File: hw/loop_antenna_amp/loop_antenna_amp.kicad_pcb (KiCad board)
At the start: 2 copper layers, 88.9 x 78.7 mm, 87 parts, among them J1 ANT1, J2 ANT2, J3 GND, J4 Coax (SMA), Q1 MMBT3904, Q2 MMBT3904, Q3 MMBT3904, Q4 MMBT3904, Q5 PZT3904, Q6 PZT3904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

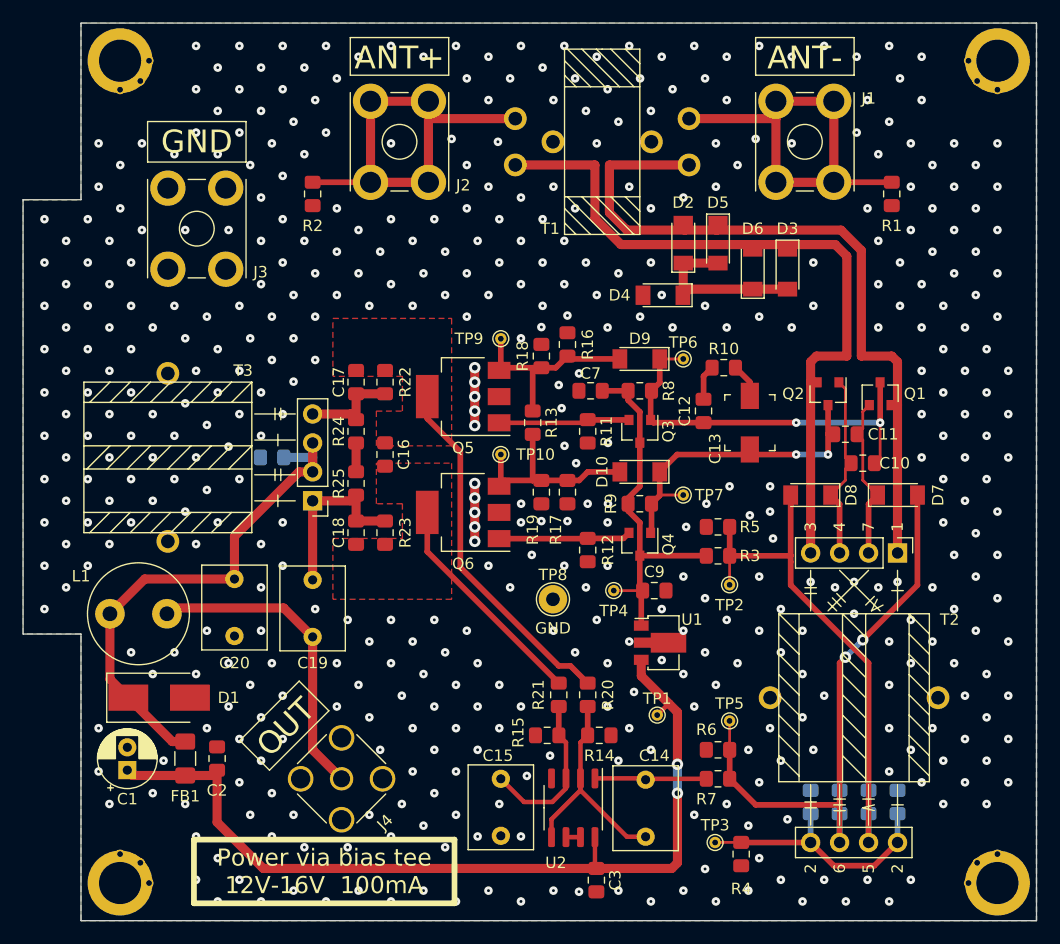
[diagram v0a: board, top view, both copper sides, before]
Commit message: Loop antenna amp: fix some vias
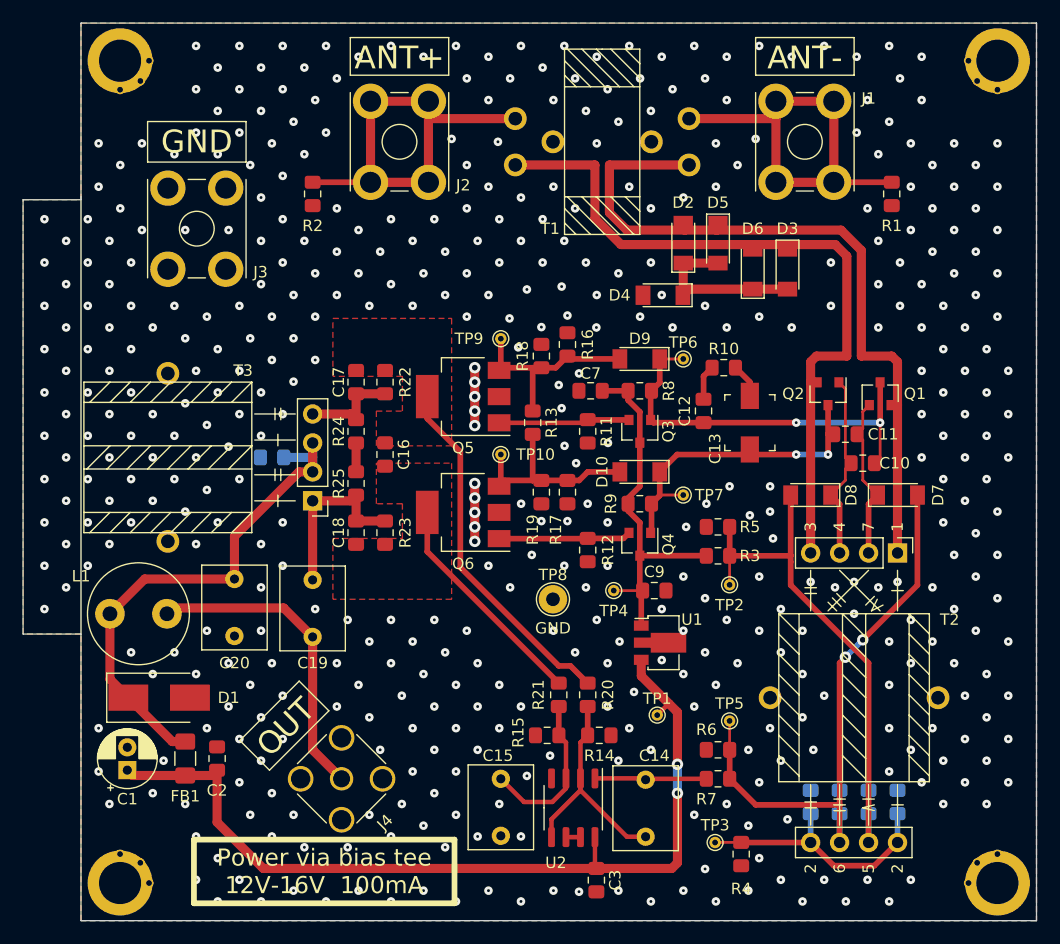
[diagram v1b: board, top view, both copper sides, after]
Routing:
- net GND: vias 483 -> 479

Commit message: Loop antenna amp: update PCB to match schematic, make it rectangular - remove fin
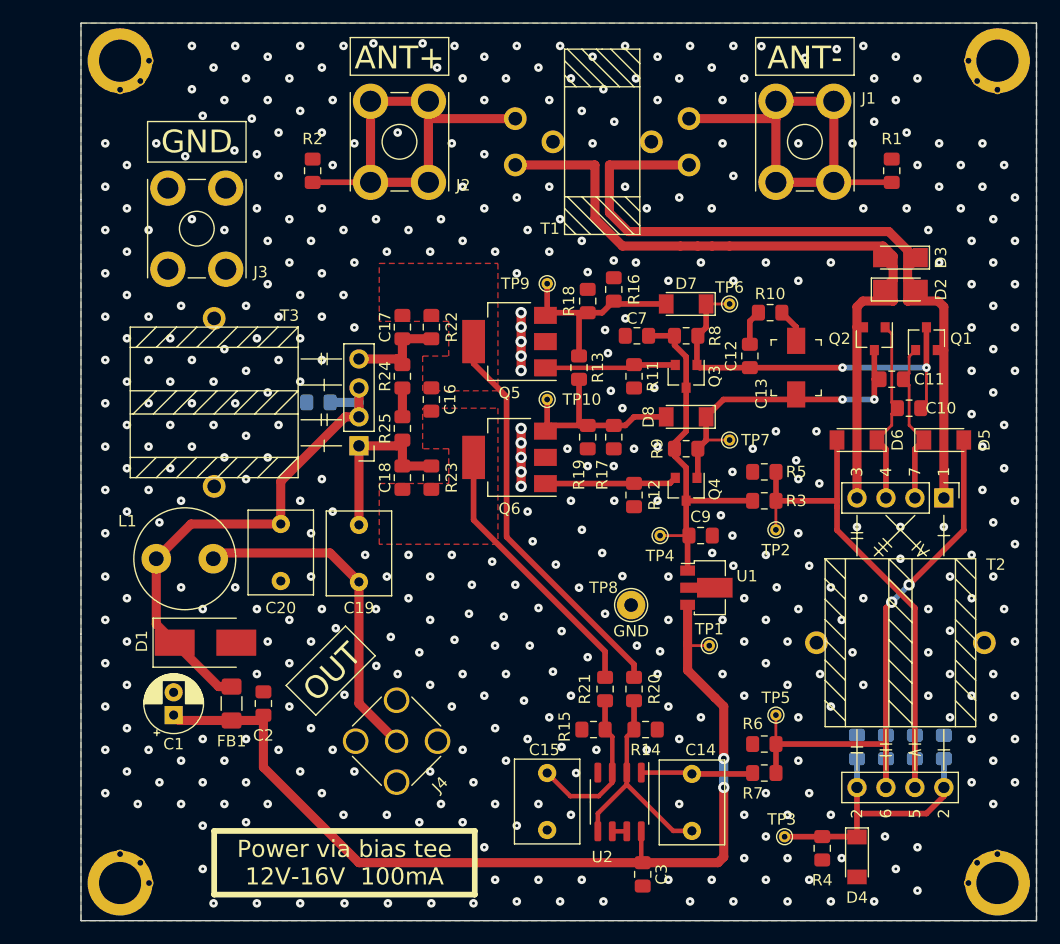
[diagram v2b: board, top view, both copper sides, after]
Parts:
- removed the D5 at (88.9, 72.4)
- removed the D6 at (91.9, 74.7)
- moved D4 52.1 mm to (101.1, 126.2), turned to 270 degrees
- moved D2 19.5 mm to (104.9, 76.5), turned to 0 degrees
- moved D3 9.96 mm to (104.9, 73.7), turned to 180 degrees
- moved TP1 7.62 mm to (88.1, 107.7)
- moved R4 7.13 mm to (98.0, 125.5)
- moved TP8 6.88 mm to (81.3, 104.1)
- moved C10 6.31 mm to (105.7, 86.9)
- moved C4 6.31 mm to (108.7, 116.6)
- moved C8 6.31 mm to (103.6, 116.6)
- moved C9 6.31 mm to (87.4, 98.0)
- moved R11 6.31 mm to (81.5, 84.1)
- moved R16 6.31 mm to (79.8, 76.5)
- moved T2 6.31 mm to (104.9, 107.4)
- moved TP10 6.31 mm to (73.9, 86.1)
- moved TP9 6.31 mm to (73.9, 75.9)
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- renumbered D7 to D5, D8 to D6, D9 to D7, D10 to D8
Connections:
- D3 pad 1: Net-(D3-Pad1) -> Net-(D2-Pad2)
- D4 pad 1: Net-(D2-Pad1) -> Net-(C4-Pad1)
- Q2 pad 2: Net-(D3-Pad1) -> Net-(D2-Pad1)
- T1 pad 3: Net-(D3-Pad1) -> Net-(D2-Pad1)
- T2 pad 3: Net-(D3-Pad1) -> Net-(D2-Pad1)
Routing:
- net Net-(D3-Pad1): track 65.6 -> 0.00 mm
- net Net-(D2-Pad1): track 15.3 -> 68.4 mm
- net VCC: track 78.5 -> 85.1 mm
- net Net-(C16-Pad2): track 19.8 -> 24.1 mm
- net Net-(D2-Pad2): track 66.0 -> 69.8 mm
- net Net-(C16-Pad1): track 31.6 -> 35.3 mm
- net Net-(C4-Pad1): track 22.8 -> 24.8 mm
- net Net-(C19-Pad1): track 27.5 -> 29.4 mm
- net Net-(C8-Pad1): track 51.5 -> 50.6 mm
- net GND: vias 479 -> 440
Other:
- board size 88.9 x 78.7 mm -> 83.8 x 78.7 mm

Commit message: Loop antenna amp: minor fixes of vias and silkscreen
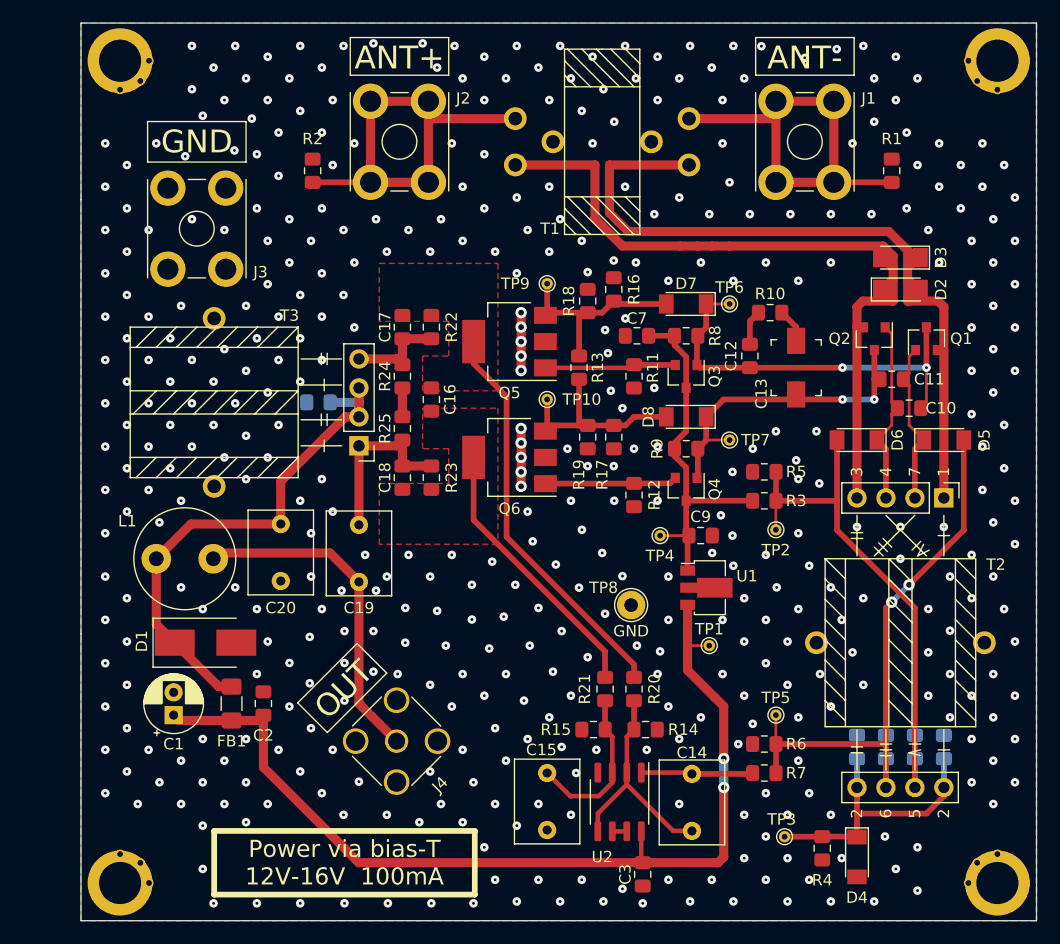
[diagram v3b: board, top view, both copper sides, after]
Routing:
- net GND: vias 440 -> 447
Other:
- board text added: "Power via bias-T 12V-16V 100mA"
- board text removed: "Power via bias tee 12V-16V 100mA"

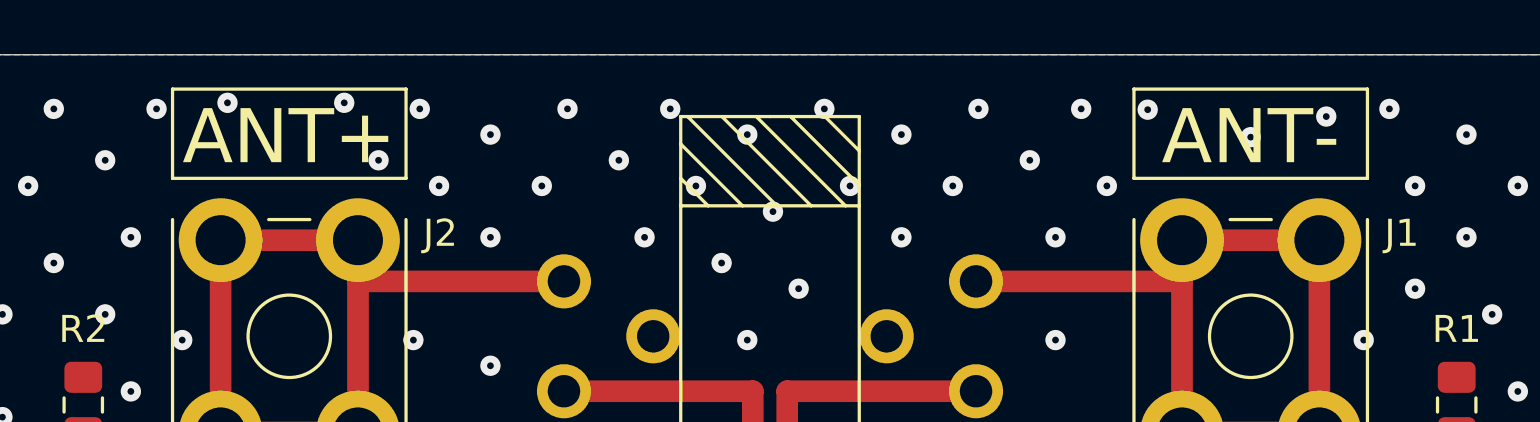
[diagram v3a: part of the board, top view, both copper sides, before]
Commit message: Loop antenna amp: fix antenna connector polarity markings
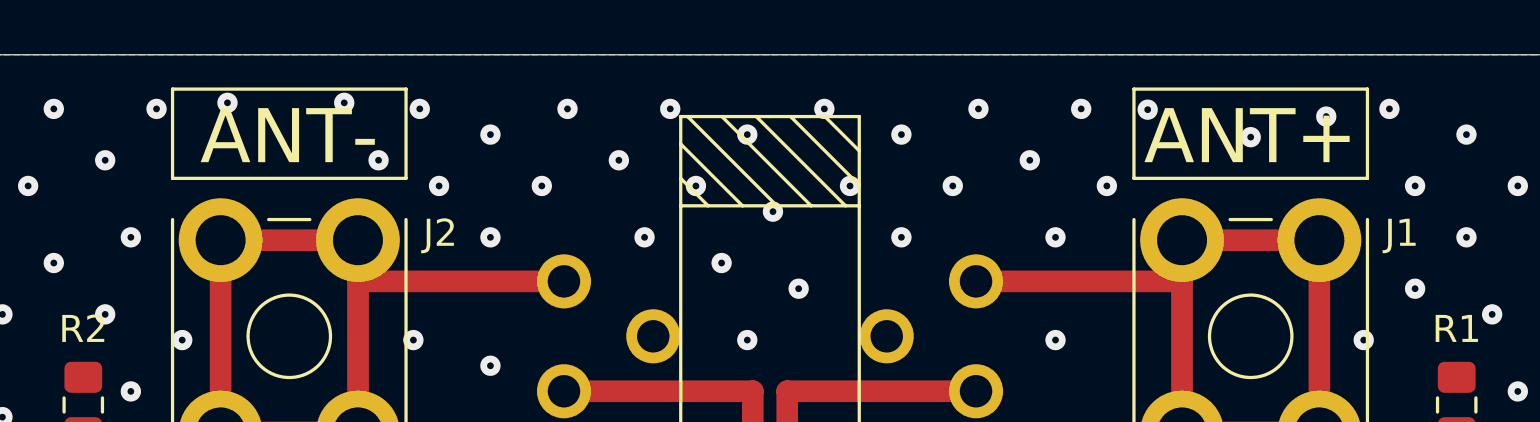
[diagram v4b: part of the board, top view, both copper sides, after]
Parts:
- J1: value ANT1 -> ANT+
- J2: value ANT2 -> ANT-
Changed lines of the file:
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@@
       (effects (font (size 1 1) (thickness 0.15)))
     )
-    (fp_text value ANT2 (at 0 -0.5) (layer F.Fab)
+    (fp_text value ANT- (at 0 -0.5) (layer F.Fab)
       (effects (font (size 1 1) (thickness 0.15)))
     )
@@
       (effects (font (size 1 1) (thickness 0.15)))
     )
-    (fp_text value ANT1 (at 0 -0.5) (layer F.Fab)
+    (fp_text value ANT+ (at 0 -0.5) (layer F.Fab)
       (effects (font (size 1 1) (thickness 0.15)))
     )
@@
   (gr_line (start 65.278 57.658) (end 56.642 57.658) (layer F.SilkS) (width 0.12))
   (gr_line (start 56.642 54.356) (end 65.278 54.356) (layer F.SilkS) (width 0.12))
-  (gr_text ANT+ (at 60.96 56.134) (layer F.SilkS)
+  (gr_text ANT- (at 60.96 56.134) (layer F.SilkS)
     (effects (font (size 2 2) (thickness 0.15)))
   )
@@
   (gr_line (start 100.838 54.356) (end 100.838 57.658) (layer F.SilkS) (width 0.12))
   (gr_line (start 92.202 54.356) (end 100.838 54.356) (layer F.SilkS) (width 0.12))
-  (gr_text ANT- (at 96.52 56.134) (layer F.SilkS)
+  (gr_text ANT+ (at 96.52 56.134) (layer F.SilkS)
     (effects (font (size 2 2) (thickness 0.15)))
   )
